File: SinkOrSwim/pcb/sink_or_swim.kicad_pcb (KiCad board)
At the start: 2 copper layers, 42.7 x 68.1 mm, 23 parts, among them P101 CONN_01X02, P102 CONN_01X03, P103 CONN_01X02, P201 CONN_01X01, Q201 BUK9575-100A, U201 LMV358, U401 LM2931

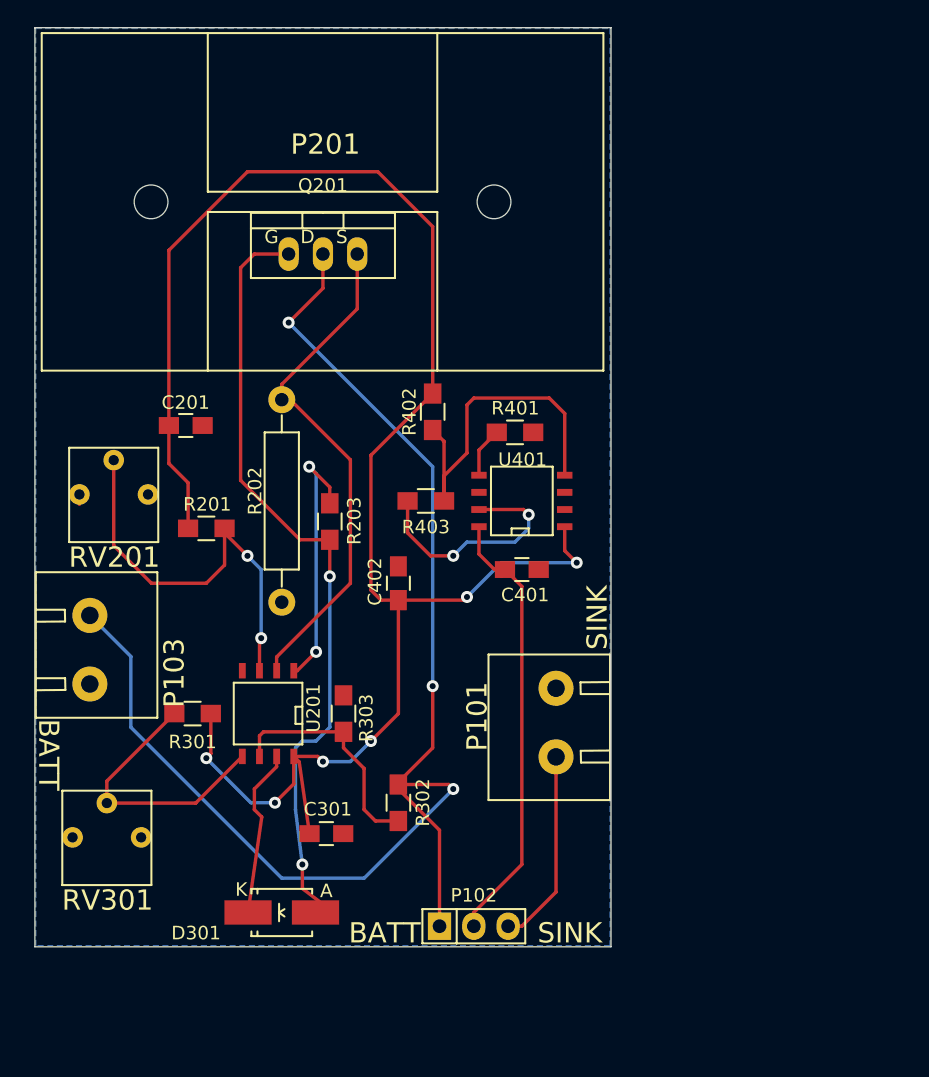
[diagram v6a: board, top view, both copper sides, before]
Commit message: More pcb layout changes.  Looks better now.
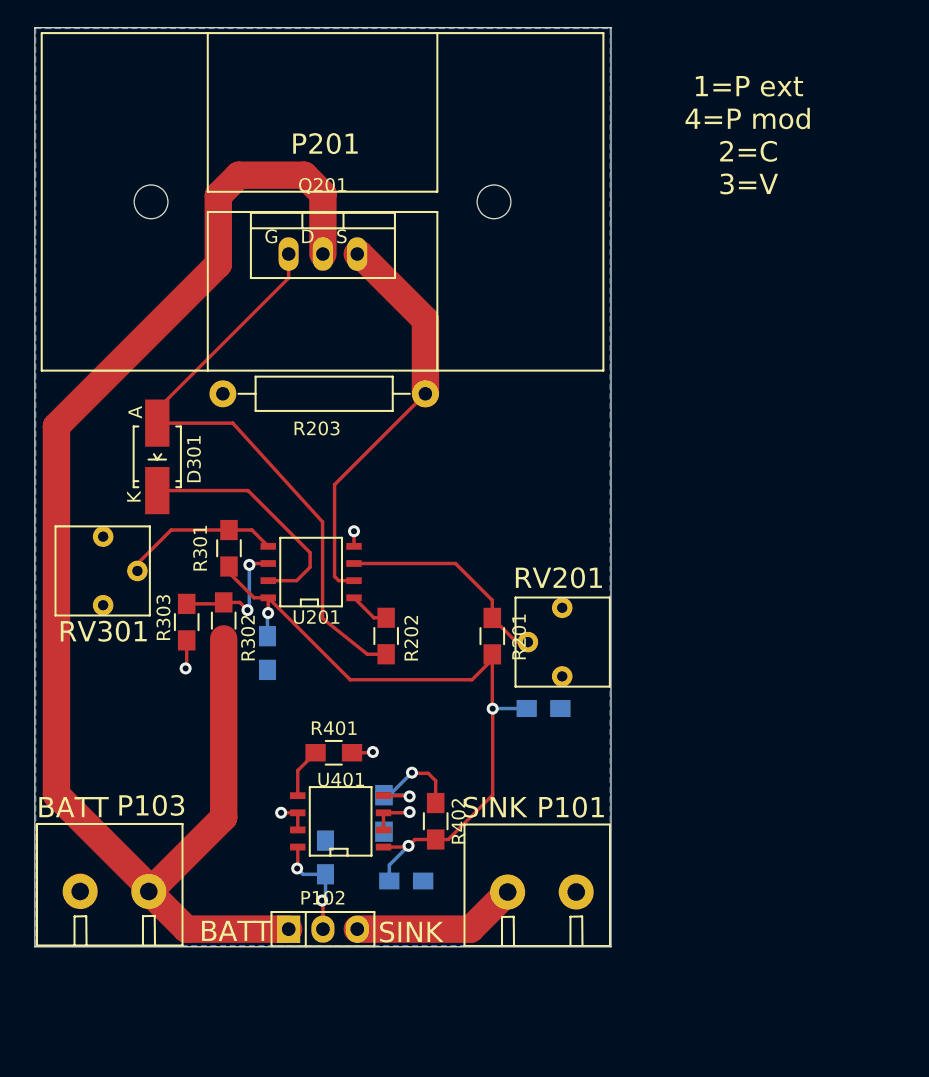
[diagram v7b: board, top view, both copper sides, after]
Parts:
- C201, C301, C401, C402, R403: moved to B.Cu
- moved RV201 41.5 mm to (191.9, 116.4), turned to 90 degrees
- moved D301 35.0 mm to (158.4, 99.3), turned to 270 degrees
- moved C201 33.8 mm to (187.0, 118.0)
- moved R402 30.3 mm to (179.0, 126.3), turned to 270 degrees
- moved R401 27.3 mm to (171.5, 121.3)
- moved U401 27.3 mm to (172.0, 126.3)
- moved RV301 26.6 mm to (150.9, 104.5), turned to 270 degrees
- moved C401 25.8 mm to (170.9, 129.0), turned to 90 degrees
- moved R403 23.4 mm to (175.2, 125.8), turned to 270 degrees
- moved R201 22.6 mm to (183.2, 112.6), turned to 90 degrees
- moved C402 22.1 mm to (176.9, 130.8), turned to 0 degrees
- moved R302 18.7 mm to (163.3, 111.5), turned to 90 degrees
- moved P103 17.8 mm to (154.9, 131.0), turned to 0 degrees
- moved C301 14.1 mm to (166.6, 113.9), turned to 270 degrees
- moved R303 13.4 mm to (160.6, 111.6), turned to 270 degrees
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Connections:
- P103 pad 1: /CurrentControl/Current_Sink+ -> GND
- P103 pad 2: GND -> /CurrentControl/Current_Sink+
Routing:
- net 2.7V: track 131.7 -> 52.9 mm, vias 6 -> 3
- net /Power Regulation/Vin: track 33.4 -> 8.07 mm, vias 0 -> 2
- net Net-(R202-Pad2): track 19.5 -> 2.99 mm, vias 2 -> 0
- net Net-(R402-Pad1): track 25.9 -> 10.3 mm, vias 0 -> 2
- net Net-(R201-Pad2): track 30.7 -> 16.1 mm, vias 2 -> 0
- net /CurrentControl/FET_Gate: track 58.2 -> 44.8 mm, vias 2 -> 0
- net Net-(R301-Pad2): track 20.2 -> 11.8 mm
- net GND: track 18.5 -> 10.9 mm, vias 2 -> 5
- net Net-(R302-Pad2): track 17.2 -> 9.63 mm, vias 0 -> 2
- net Net-(Q201-PadS): track 37.9 -> 30.4 mm
- net Net-(D301-Pad2): track 12.5 -> 17.8 mm
- net /CurrentControl/Current_Sink+: track 102.6 -> 105.3 mm, vias 3 -> 0
- net Net-(P101-Pad1): track 14.6 -> 12.3 mm
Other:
- net class PWR added: clearance 0.254, trace_width 2.03, via_dia 2.03, via_drill 1.8
- board text added: "1=P ext 4=P mod 2=C 3=V"

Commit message: Updated Design Rules for power on pcb and redrew some traces.
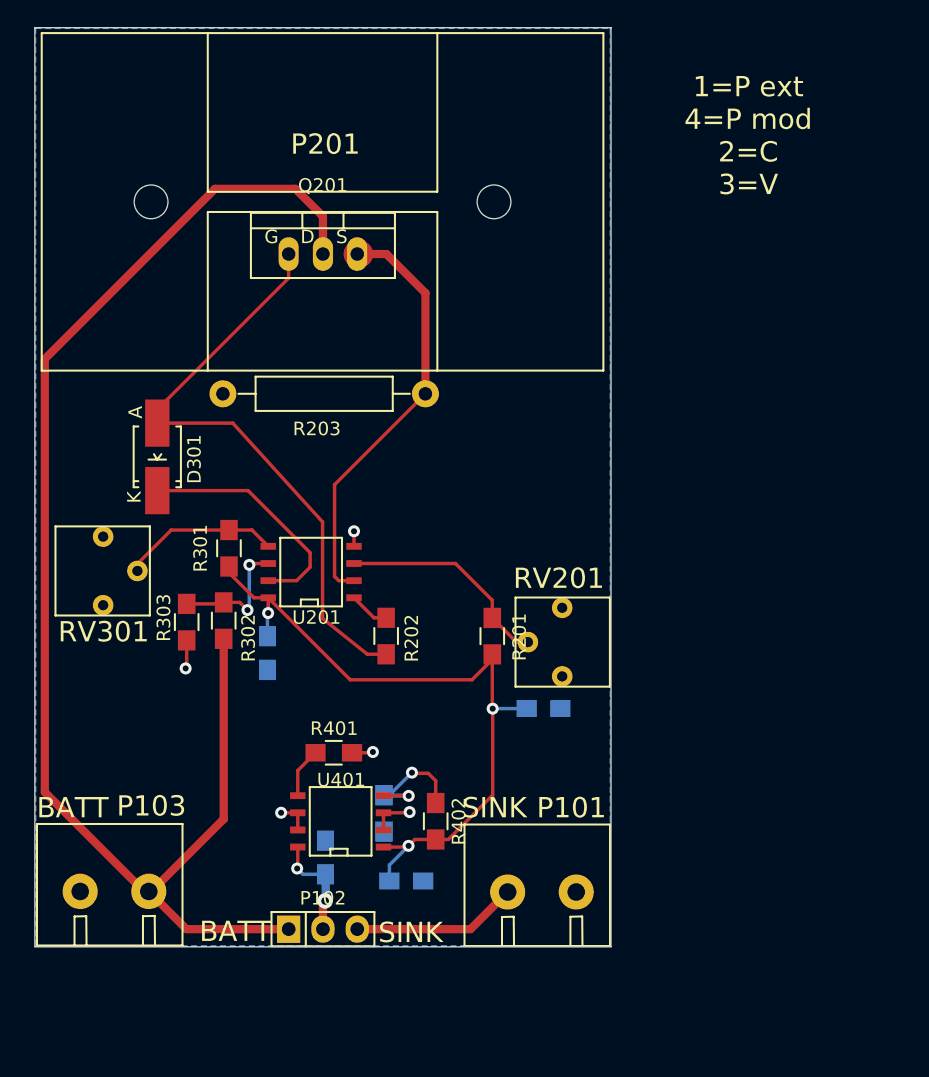
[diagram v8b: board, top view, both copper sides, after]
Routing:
- net Net-(R402-Pad1): track 10.3 -> 12.0 mm
- net Net-(Q201-PadS): track 30.4 -> 31.8 mm
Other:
- net class PWR: clearance 0.254 -> 0.305; trace_width 2.03 -> 0.61; via_dia 2.03 -> 1.143; via_drill 1.8 -> 0.762
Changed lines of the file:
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@@
     (links 44)
     (no_connects 0)
-    (area 147.451001 67.513999 207.661429 138.179)
+    (area 147.400001 67.513999 207.661429 138.23)
     (thickness 1.6)
     (drawings 9)
-    (tracks 127)
+    (tracks 130)
     (zones 0)
     (modules 23)
@@
     (uvia_drill 0.127)
     (add_net /CurrentControl/FET_Gate)
-    (add_net "/Power Regulation/Vin")
-    (add_net 2.7V)
-    (add_net GND)
     (add_net "Net-(D301-Pad2)")
     (add_net "Net-(R201-Pad2)")
@@
   )
   (net_class PWR ""
-    (clearance 0.254)
-    (trace_width 2.03)
-    (via_dia 2.03)
-    (via_drill 1.8)
+    (clearance 0.305)
+    (trace_width 0.61)
+    (via_dia 1.143)
+    (via_drill 0.762)
     (uvia_dia 0.508)
     (uvia_drill 0.127)
     (add_net /CurrentControl/Current_Sink+)
+    (add_net "/Power Regulation/Vin")
+    (add_net 2.7V)
+    (add_net GND)
     (add_net "Net-(P101-Pad1)")
     (add_net "Net-(Q201-PadS)")
@@
   (segment (start 177.059 125.711) (end 177.11 125.66) (width 0.254) (layer F.Cu) (net 2))
   (segment (start 152.71 131.54) (end 152.71 131.21) (width 2.03) (layer F.Cu) (net 2))
+  (segment (start 170.88 130.27) (end 170.88 132.21) (width 0.61) (layer B.Cu) (net 3))
+  (segment (start 170.69 132.4) (end 170.69 134.33) (width 0.61) (layer F.Cu) (net 3))
+  (segment (start 170.85 132.24) (end 170.69 132.4) (width 0.61) (layer F.Cu) (net 3))
+  (via (at 170.85 132.24) (size 1.143) (layers F.Cu B.Cu) (net 3))
+  (segment (start 170.88 132.21) (end 170.85 132.24) (width 0.61) (layer B.Cu) (net 3))
   (segment (start 168.825 128.251) (end 168.825 129.795) (width 0.254) (layer F.Cu) (net 3))
   (segment (start 169.21 130.27) (end 170.88 130.27) (width 0.254) (layer B.Cu) (net 3))
@@
   (via (at 168.78 129.84) (size 0.889) (layers F.Cu B.Cu) (net 3))
   (segment (start 168.825 129.795) (end 168.78 129.84) (width 0.254) (layer F.Cu) (net 3))
-  (segment (start 170.69 134.33) (end 170.69 132.27) (width 0.254) (layer F.Cu) (net 3))
-  (segment (start 170.88 131.96) (end 170.88 130.27) (width 0.254) (layer B.Cu) (net 3))
-  (segment (start 170.63 132.21) (end 170.88 131.96) (width 0.254) (layer B.Cu) (net 3))
-  (via (at 170.63 132.21) (size 0.889) (layers F.Cu B.Cu) (net 3))
-  (segment (start 170.69 132.27) (end 170.63 132.21) (width 0.254) (layer F.Cu) (net 3))
   (segment (start 158.42 96.85064) (end 158.42 95.84) (width 0.254) (layer F.Cu) (net 4))
   (segment (start 158.42 95.84) (end 168.148 86.112) (width 0.254) (layer F.Cu) (net 4))
@@
   (segment (start 169.74 107.52) (end 169.74 106.45) (width 0.254) (layer F.Cu) (net 5))
   (segment (start 168.741 108.519) (end 169.74 107.52) (width 0.254) (layer F.Cu) (net 5))
-  (segment (start 173.23 134.33) (end 181.62 134.33) (width 2.03) (layer F.Cu) (net 6))
-  (segment (start 181.62 134.33) (end 184.37 131.58) (width 2.03) (layer F.Cu) (net 6))
+  (segment (start 173.23 134.33) (end 181.62 134.33) (width 0.61) (layer F.Cu) (net 6))
+  (segment (start 181.62 134.33) (end 184.37 131.58) (width 0.61) (layer F.Cu) (net 6))
+  (segment (start 157.79 131.54) (end 157.45 131.54) (width 0.61) (layer F.Cu) (net 7))
+  (segment (start 157.45 131.54) (end 150.09 124.18) (width 0.61) (layer F.Cu) (net 7))
+  (segment (start 170.688 81.538) (end 170.688 84.328) (width 0.61) (layer F.Cu) (net 7))
+  (segment (start 168.65 79.5) (end 170.688 81.538) (width 0.61) (layer F.Cu) (net 7))
+  (segment (start 162.69 79.5) (end 168.65 79.5) (width 0.61) (layer F.Cu) (net 7))
+  (segment (start 150.09 92.1) (end 162.69 79.5) (width 0.61) (layer F.Cu) (net 7))
+  (segment (start 150.09 124.18) (end 150.09 92.1) (width 0.61) (layer F.Cu) (net 7))
+  (segment (start 168.15 134.33) (end 160.58 134.33) (width 0.61) (layer F.Cu) (net 7))
+  (segment (start 160.58 134.33) (end 157.79 131.54) (width 0.61) (layer F.Cu) (net 7))
   (segment (start 157.79 131.54) (end 157.86 131.54) (width 2.03) (layer F.Cu) (net 7))
-  (segment (start 157.86 131.54) (end 163.34 126.06) (width 2.03) (layer F.Cu) (net 7))
-  (segment (start 163.34 126.06) (end 163.34 112.83) (width 2.03) (layer F.Cu) (net 7))
   (segment (start 157.79 131.54) (end 157.79 131.21) (width 2.03) (layer F.Cu) (net 7))
-  (segment (start 157.79 131.21) (end 150.95 124.37) (width 2.03) (layer F.Cu) (net 7))
-  (segment (start 170.688 79.878) (end 170.688 84.328) (width 2.03) (layer F.Cu) (net 7))
-  (segment (start 169.3 78.49) (end 170.688 79.878) (width 2.03) (layer F.Cu) (net 7))
-  (segment (start 164.46 78.49) (end 169.3 78.49) (width 2.03) (layer F.Cu) (net 7))
-  (segment (start 162.94 80.01) (end 164.46 78.49) (width 2.03) (layer F.Cu) (net 7))
-  (segment (start 162.94 85.09) (end 162.94 80.01) (width 2.03) (layer F.Cu) (net 7))
-  (segment (start 150.95 97.08) (end 162.94 85.09) (width 2.03) (layer F.Cu) (net 7))
-  (segment (start 150.95 124.37) (end 150.95 97.08) (width 2.03) (layer F.Cu) (net 7))
-  (segment (start 168.15 134.33) (end 160.58 134.33) (width 2.03) (layer F.Cu) (net 7))
-  (segment (start 160.58 134.33) (end 157.79 131.54) (width 2.03) (layer F.Cu) (net 7))
+  (segment (start 163.34 126.18) (end 163.34 112.83) (width 0.61) (layer F.Cu) (net 7))
+  (segment (start 157.98 131.54) (end 163.34 126.18) (width 0.61) (layer F.Cu) (net 7))
+  (segment (start 157.79 131.54) (end 157.98 131.54) (width 0.61) (layer F.Cu) (net 7))
+  (segment (start 173.228 84.328) (end 175.388 84.328) (width 0.61) (layer F.Cu) (net 8))
+  (segment (start 178.28 87.22) (end 178.28 94.68) (width 0.61) (layer F.Cu) (net 8))
+  (segment (start 175.388 84.328) (end 178.28 87.22) (width 0.61) (layer F.Cu) (net 8))
   (segment (start 173.228 84.328) (end 173.398 84.328) (width 2.03) (layer F.Cu) (net 8))
-  (segment (start 173.398 84.328) (end 178.28 89.21) (width 2.03) (layer F.Cu) (net 8))
-  (segment (start 178.28 89.21) (end 178.28 94.68) (width 2.03) (layer F.Cu) (net 8))
   (segment (start 172.989 108.519) (end 171.859 108.519) (width 0.254) (layer F.Cu) (net 8))
+  (segment (start 171.859 108.519) (end 171.55 108.21) (width 0.254) (layer F.Cu) (net 8))
+  (segment (start 171.55 108.21) (end 171.55 101.41) (width 0.254) (layer F.Cu) (net 8))
   (segment (start 171.55 101.41) (end 178.28 94.68) (width 0.254) (layer F.Cu) (net 8))
-  (segment (start 171.55 108.21) (end 171.55 101.41) (width 0.254) (layer F.Cu) (net 8))
-  (segment (start 171.859 108.519) (end 171.55 108.21) (width 0.254) (layer F.Cu) (net 8))
   (segment (start 175.37 111.27) (end 174.47 111.27) (width 0.254) (layer F.Cu) (net 9))
   (segment (start 174.47 111.27) (end 172.989 109.789) (width 0.254) (layer F.Cu) (net 9))
@@
   (segment (start 168.825 124.441) (end 168.825 122.583) (width 0.254) (layer F.Cu) (net 11))
   (segment (start 168.825 122.583) (end 170.142 121.266) (width 0.254) (layer F.Cu) (net 11))
+  (segment (start 175.21 124.41) (end 176.99 124.41) (width 0.254) (layer B.Cu) (net 12))
+  (segment (start 176.99 124.41) (end 177.04 124.46) (width 0.254) (layer B.Cu) (net 12))
+  (segment (start 175.26 124.46) (end 177.04 124.46) (width 0.254) (layer B.Cu) (net 12))
+  (segment (start 177.021 124.441) (end 177.04 124.46) (width 0.254) (layer F.Cu) (net 12))
+  (segment (start 177.021 124.441) (end 175.175 124.441) (width 0.254) (layer F.Cu) (net 12))
+  (via (at 177.04 124.46) (size 0.889) (layers F.Cu B.Cu) (net 12))
+  (segment (start 175.26 124.46) (end 175.21 124.41) (width 0.254) (layer B.Cu) (net 12))
   (segment (start 175.21 124.41) (end 175.61 124.41) (width 0.254) (layer B.Cu) (net 12))
   (segment (start 175.61 124.41) (end 177.28 122.74) (width 0.254) (layer B.Cu) (net 12))
@@
   (segment (start 177.28 122.74) (end 177.33 122.79) (width 0.254) (layer F.Cu) (net 12))
   (via (at 177.28 122.74) (size 0.889) (layers F.Cu B.Cu) (net 12))
-  (segment (start 175.175 124.441) (end 177.051 124.441) (width 0.254) (layer F.Cu) (net 12))
-  (segment (start 177.02 124.41) (end 175.21 124.41) (width 0.254) (layer B.Cu) (net 12))
-  (segment (start 177.11 124.5) (end 177.02 124.41) (width 0.254) (layer B.Cu) (net 12))
-  (via (at 177.11 124.5) (size 0.889) (layers F.Cu B.Cu) (net 12))
-  (segment (start 177.051 124.441) (end 177.11 124.5) (width 0.254) (layer F.Cu) (net 12))
   (segment (start 183.23 111.28) (end 183.23 109.97) (width 0.254) (layer F.Cu) (net 15))
   (segment (start 180.509 107.249) (end 172.989 107.249) (width 0.254) (layer F.Cu) (net 15))
